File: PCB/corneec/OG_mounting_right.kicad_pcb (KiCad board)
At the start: 2 copper layers, 133.7 x 91.4 mm, 53 parts, among them J1 OLED, J2 MJ-4PP-9, Q1 Q_NMOS_GSD, SW1 SW_Push, SW10 EC_SW, SW11 EC_SW, SW12 EC_SW, SW13 EC_SW, SW14 EC_SW, SW15 EC_SW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

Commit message: Update of rev commit to include extra screw mount
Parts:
- added ?: , kbd:LEGO_HOLE, B.Cu at (157.1, 76.6)
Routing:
- net GNDA: vias 81 -> 91
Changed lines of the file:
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@@
       (drillshape 0)
       (scaleselection 1)
-      (outputdirectory "OG")
+      (outputdirectory "OG_right")
     )
   )
@@
     )
   )
+  (footprint "kbd:LEGO_HOLE" (layer "B.Cu")
+    (at 157.1264 76.6462 180)
+    (descr "Mounting Hole 2.2mm, no annular, M2")
+    (tags "mounting hole 2.2mm no annular m2")
+    (attr exclude_from_pos_files exclude_from_bom)
+    (fp_text reference "" (at 0 3.2) (layer "B.SilkS")
+      (effects (font (size 1 1) (thickness 0.15)) (justify mirror))
+    )
+    (fp_text value "" (at 0 -3.2) (layer "B.Fab")
+      (effects (font (size 1 1) (thickness 0.15)) (justify mirror))
+    )
+    (fp_text user "${REFERENCE}" (at 0.3 0) (layer "B.Fab")
+      (effects (font (size 1 1) (thickness 0.15)) (justify mirror))
+    )
+    (fp_circle (center 0 0) (end 2.2 0) (layer "Cmts.User") (width 0.15) (fill none))
+    (fp_circle (center 0 0) (end 2.45 0) (layer "B.CrtYd") (width 0.05) (fill none))
+    (pad "" thru_hole circle locked (at 0 0 180) (size 4 4) (drill 2.2) (layers *.Cu *.Mask)
+      (net 1 "GNDA"))
+  )
   (footprint "cipulot_parts:R_0603_1608Metric_Pad0.98x0.95mm_HandSolder" (layer "B.Cu")
     (at 164.725 77.8212 180)
@@
   (gr_circle (center 138.125 125.95) (end 132.133 125.95) (layer "B.Cu") (width 0.01) (fill none))
   (gr_circle (center 117.125 128.7) (end 111.133 128.7) (layer "B.Cu") (width 0.01) (fill none))
-  (gr_circle (center 147.625 65.95) (end 141.633 65.95) (layer "B.Cu") (width 0.01) (fill none))
+  (gr_circle (center 147.625 65.95) (end 153.617 65.95) (layer "B.Cu") (width 0.01) (fill none))
   (gr_circle (center 128.625 87.325) (end 122.633 87.325) (layer "B.Cu") (width 0.01) (fill none))
   (gr_circle (center 166.625 68.325) (end 160.633 68.325) (layer "B.Cu") (width 0.01) (fill none))
@@
   (segment (start 120.85 114.25) (end 120.85 118.875) (width 0.25) (layer "F.Cu") (net 1))
   (segment (start 119.8 113.2) (end 120.85 114.25) (width 0.25) (layer "F.Cu") (net 1))
-  (via (at 150.025 75.45) (size 0.8) (drill 0.4) (layers "F.Cu" "B.Cu") (free) (net 1))
+  (via (at 149.025 75.45) (size 0.8) (drill 0.4) (layers "F.Cu" "B.Cu") (free) (net 1))
   (via (at 154.85 91.825) (size 0.8) (drill 0.4) (layers "F.Cu" "B.Cu") (free) (net 1))
   (via (at 128.8 123.375) (size 0.8) (drill 0.4) (layers "F.Cu" "B.Cu") (free) (net 1))
-  (via (at 161 77.85) (size 0.8) (drill 0.4) (layers "F.Cu" "B.Cu") (free) (net 1))
+  (via (at 161.275 77.825) (size 0.8) (drill 0.4) (layers "F.Cu" "B.Cu") (free) (net 1))
   (via (at 161.325 113.1) (size 0.8) (drill 0.4) (layers "F.Cu" "B.Cu") (free) (net 1))
+  (via (at 179.675 103.65) (size 0.8) (drill 0.4) (layers "F.Cu" "B.Cu") (free) (net 1))
   (via (at 102.725 77.925) (size 0.8) (drill 0.4) (layers "F.Cu" "B.Cu") (free) (net 1))
   (via (at 85.425 131.65) (size 0.8) (drill 0.4) (layers "F.Cu" "B.Cu") (free) (net 1))
@@
   (via (at 121.85 111.6) (size 0.8) (drill 0.4) (layers "F.Cu" "B.Cu") (free) (net 1))
   (via (at 109.475 124.225) (size 0.8) (drill 0.4) (layers "F.Cu" "B.Cu") (free) (net 1))
+  (via (at 141.975 92.6) (size 0.8) (drill 0.4) (layers "F.Cu" "B.Cu") (free) (net 1))
   (via (at 101.9 136.125) (size 0.8) (drill 0.4) (layers "F.Cu" "B.Cu") (net 1))
   (via (at 132.025 77.725) (size 0.8) (drill 0.4) (layers "F.Cu" "B.Cu") (free) (net 1))
@@
   (via (at 173.9128 60.7664) (size 0.8) (drill 0.4) (layers "F.Cu" "B.Cu") (free) (net 1))
   (via (at 109.675 121.075) (size 0.8) (drill 0.4) (layers "F.Cu" "B.Cu") (free) (net 1))
+  (via (at 141.975 96.35) (size 0.8) (drill 0.4) (layers "F.Cu" "B.Cu") (free) (net 1))
   (via (at 172.9 101.225) (size 0.8) (drill 0.4) (layers "F.Cu" "B.Cu") (net 1))
   (via (at 154.8 97.675) (size 0.8) (drill 0.4) (layers "F.Cu" "B.Cu") (free) (net 1))
@@
   (via (at 153.4 123.175) (size 0.8) (drill 0.4) (layers "F.Cu" "B.Cu") (free) (net 1))
   (via (at 177.291 65.4908) (size 0.8) (drill 0.4) (layers "F.Cu" "B.Cu") (free) (net 1))
+  (via (at 152.775 74.4) (size 0.8) (drill 0.4) (layers "F.Cu" "B.Cu") (free) (net 1))
   (via (at 137.4 106.8) (size 0.8) (drill 0.4) (layers "F.Cu" "B.Cu") (free) (net 1))
   (via (at 117.3 95.95) (size 0.8) (drill 0.4) (layers "F.Cu" "B.Cu") (free) (net 1))
+  (via (at 161.225 98.55) (size 0.8) (drill 0.4) (layers "F.Cu" "B.Cu") (free) (net 1))
   (via (at 122.075 98.475) (size 0.8) (drill 0.4) (layers "F.Cu" "B.Cu") (free) (net 1))
+  (via (at 206.025 103.125) (size 0.8) (drill 0.4) (layers "F.Cu" "B.Cu") (net 1))
   (via (at 199.2112 82.5596) (size 0.8) (drill 0.4) (layers "F.Cu" "B.Cu") (free) (net 1))
   (via (at 135.825 92.925) (size 0.8) (drill 0.4) (layers "F.Cu" "B.Cu") (free) (net 1))
   (via (at 102.225 63.25) (size 0.8) (drill 0.4) (layers "F.Cu" "B.Cu") (free) (net 1))
   (via (at 102.65 82.675) (size 0.8) (drill 0.4) (layers "F.Cu" "B.Cu") (free) (net 1))
+  (via (at 179.75 99.825) (size 0.8) (drill 0.4) (layers "F.Cu" "B.Cu") (free) (net 1))
   (via (at 155.75 83.575) (size 0.8) (drill 0.4) (layers "F.Cu" "B.Cu") (net 1))
   (via (at 168.825 77.85) (size 0.8) (drill 0.4) (layers "F.Cu" "B.Cu") (free) (net 1))
@@
   (via (at 206.9836 82.6104) (size 0.8) (drill 0.4) (layers "F.Cu" "B.Cu") (free) (net 1))
   (via (at 92.525 123.075) (size 0.8) (drill 0.4) (layers "F.Cu" "B.Cu") (free) (net 1))
+  (via (at 187.2 103.275) (size 0.8) (drill 0.4) (layers "F.Cu" "B.Cu") (net 1))
   (via (at 211.7334 65.7956) (size 0.8) (drill 0.4) (layers "F.Cu" "B.Cu") (free) (net 1))
+  (via (at 159.225 80.875) (size 0.8) (drill 0.4) (layers "F.Cu" "B.Cu") (free) (net 1))
   (via (at 197.325 113.775) (size 0.8) (drill 0.4) (layers "F.Cu" "B.Cu") (net 1))
   (via (at 97.575 120.45) (size 0.8) (drill 0.4) (layers "F.Cu" "B.Cu") (net 1))
@@
   (via (at 179.6786 82.5342) (size 0.8) (drill 0.4) (layers "F.Cu" "B.Cu") (free) (net 1))
   (via (at 104.575 137.925) (size 0.8) (drill 0.4) (layers "F.Cu" "B.Cu") (free) (net 1))
+  (via (at 136.85 77.875) (size 0.8) (drill 0.4) (layers "F.Cu" "B.Cu") (free) (net 1))
   (via (at 191.275 116.875) (size 0.8) (drill 0.4) (layers "F.Cu" "B.Cu") (net 1))
   (via (at 157.4028 60.5378) (size 0.8) (drill 0.4) (layers "F.Cu" "B.Cu") (free) (net 1))
@@
   (segment (start 189.55 76) (end 190.675 77.125) (width 0.25) (layer "B.Cu") (net 2))
   (segment (start 209.2188 100.6688) (end 209.2188 76.6636) (width 0.25) (layer "B.Cu") (net 2))
+  (segment (start 157.175 93.97692) (end 157.15096 94.00096) (width 0.25) (layer "B.Cu") (net 2))
   (segment (start 190.675 100.35) (end 190.675 100.775) (width 0.25) (layer "B.Cu") (net 2))
   (segment (start 174.1625 74.8625) (end 174.4 75.1) (width 0.25) (layer "B.Cu") (net 2))
-  (segment (start 157.175 93.97692) (end 157.175 74.4948) (width 0.25) (layer "B.Cu") (net 2))
   (segment (start 167.6264 68.3264) (end 174.1625 74.8625) (width 0.25) (layer "B.Cu") (net 2))
   (segment (start 138.975 110.275) (end 138.125 111.125) (width 0.25) (layer "B.Cu") (net 2))
   (segment (start 209.2188 76.6636) (end 205.6264 73.0712) (width 0.25) (layer "B.Cu") (net 2))
+  (segment (start 157.175 81.725) (end 157.175 93.97692) (width 0.25) (layer "B.Cu") (net 2))
   (segment (start 209.225 100.675) (end 209.2188 100.6688) (width 0.25) (layer "B.Cu") (net 2))
   (segment (start 138.1264 116.8014) (end 138.1264 124.9462) (width 0.25) (layer "B.Cu") (net 2))
   (segment (start 176.05 76.75) (end 176.05 98.275) (width 0.25) (layer "B.Cu") (net 2))
   (segment (start 174.1625 74.8625) (end 176.05 76.75) (width 0.25) (layer "B.Cu") (net 2))
-  (segment (start 157.15096 94.00096) (end 157.175 93.97692) (width 0.25) (layer "B.Cu") (net 2))
+  (segment (start 148.6264 73.1764) (end 157.175 81.725) (width 0.25) (layer "B.Cu") (net 2))
   (segment (start 190.675 77.125) (end 190.675 78.375) (width 0.25) (layer "B.Cu") (net 2))
   (segment (start 138.975 94.57692) (end 138.975 110.275) (width 0.25) (layer "B.Cu") (net 2))
@@
   (segment (start 129.6264 68.3212) (end 129.6264 68.3264) (width 0.25) (layer "B.Cu") (net 2))
   (segment (start 138.39904 94.00096) (end 138.975 94.57692) (width 0.25) (layer "B.Cu") (net 2))
-  (segment (start 148.6264 65.9462) (end 157.175 74.4948) (width 0.25) (layer "B.Cu") (net 2))
+  (segment (start 148.6264 65.9462) (end 148.6264 73.1764) (width 0.25) (layer "B.Cu") (net 2))
   (segment (start 167.6264 68.3212) (end 167.6264 68.3264) (width 0.25) (layer "B.Cu") (net 2))
   (segment (start 138.4 94) (end 138.39904 94.00096) (width 0.25) (layer "B.Cu") (net 2))

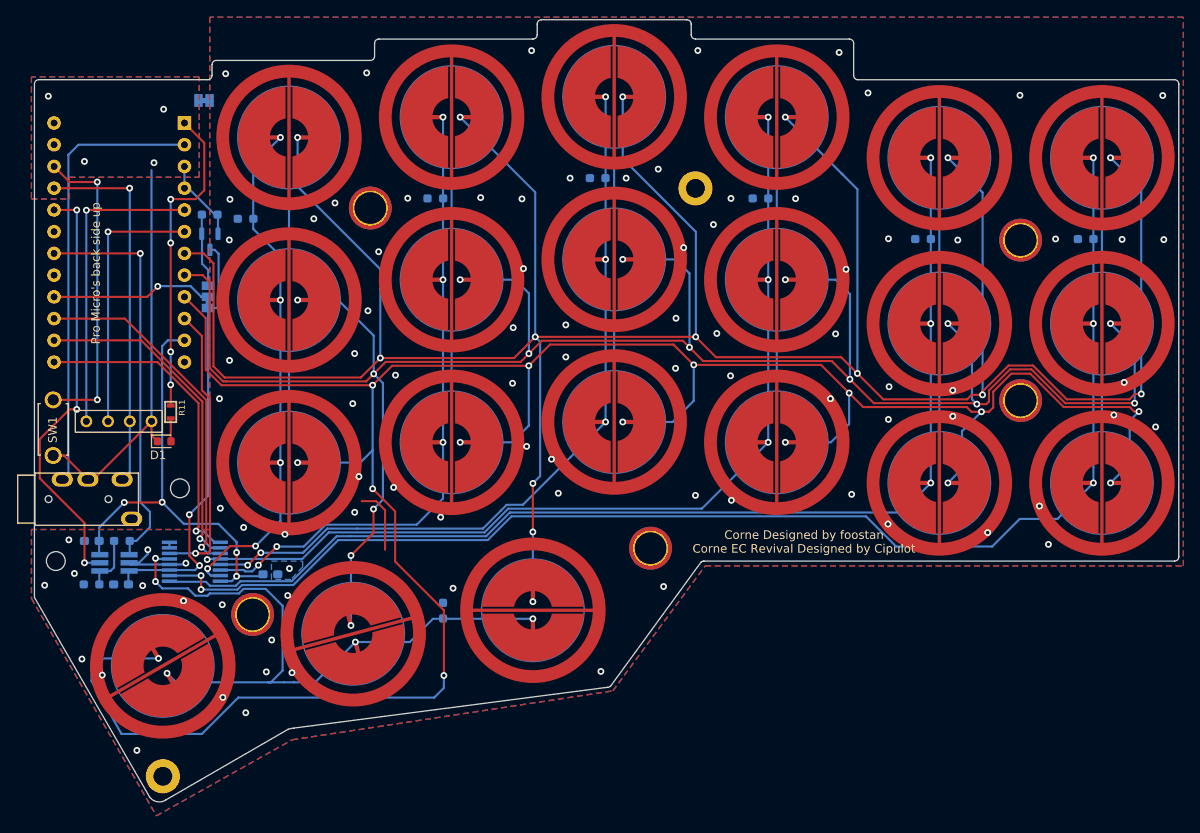
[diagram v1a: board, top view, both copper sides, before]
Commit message: Updated EC pad footprint
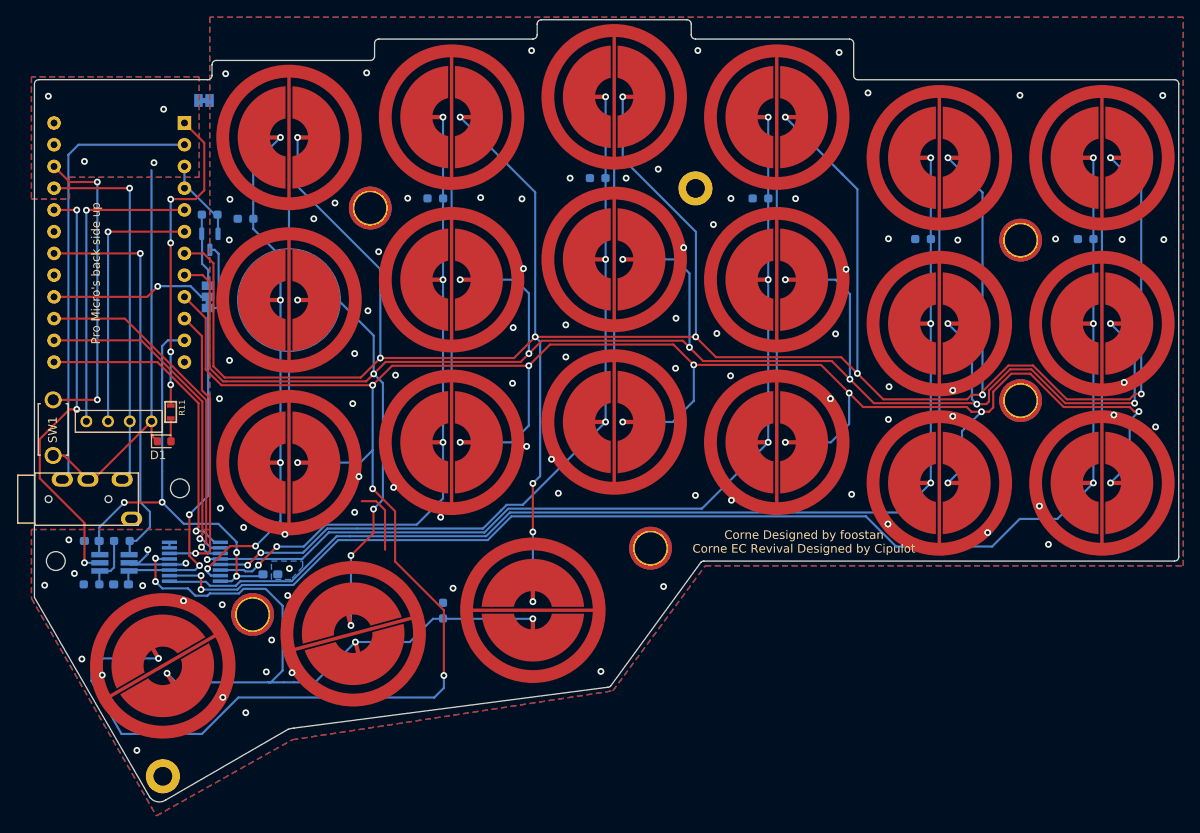
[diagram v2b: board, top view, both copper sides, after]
